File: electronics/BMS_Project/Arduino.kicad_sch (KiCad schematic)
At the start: 8 parts, among them SW1 SW_Push, SW3 SW_Push, SW4 SW_Push, SW5 SW_Push

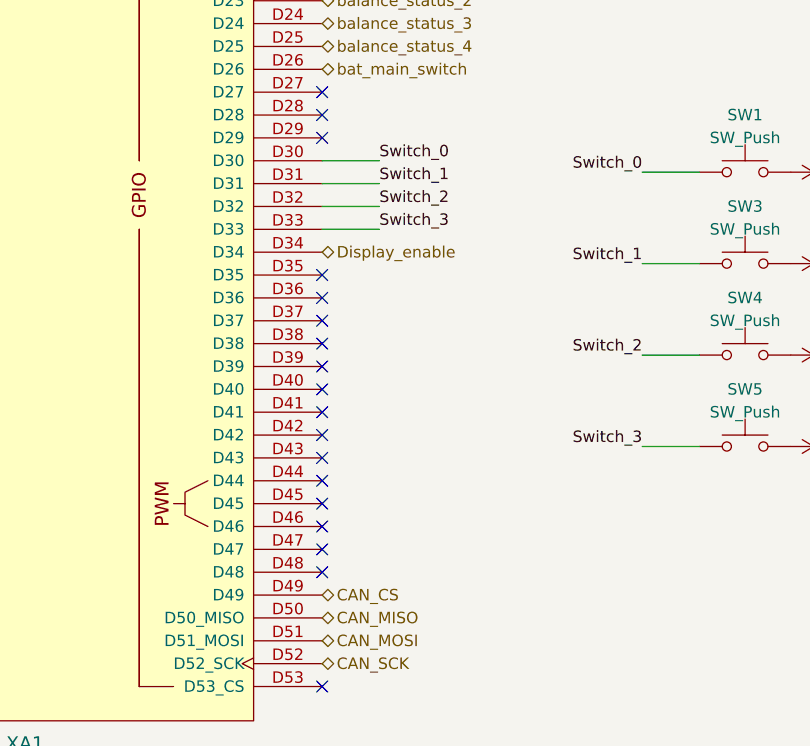
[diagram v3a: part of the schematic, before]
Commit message: Started PCB layout and adjusted schematic to suit the layout needs better
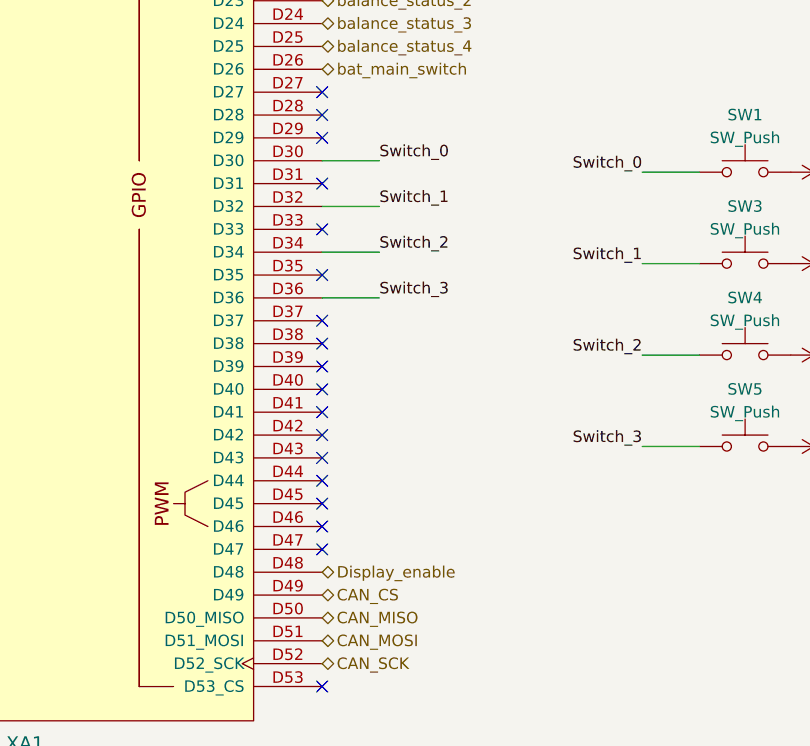
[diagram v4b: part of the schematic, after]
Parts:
- R13: footprint Resistor_THT:R_Axial_DIN0207_L6.3mm_D2.5mm_P10.16mm_Horizontal -> Resistor_SMD:R_0805_2012Metric
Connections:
- net Display_enable: now also XA1.D48; no longer XA1.D34
- net Switch_1: now also XA1.D32; no longer XA1.D31
- net Switch_2: now also XA1.D34; no longer XA1.D32
- net Switch_3: now also XA1.D36; no longer XA1.D33
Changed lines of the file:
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@@
   (no_connect (at 82.55 99.06))
   (no_connect (at 148.59 109.22))
-  (no_connect (at 148.59 137.16))
+  (no_connect (at 148.59 93.98))
   (no_connect (at 119.38 29.21))
   (no_connect (at 111.76 29.21))
@@
   (no_connect (at 148.59 53.34))
   (no_connect (at 109.22 29.21))
-  (no_connect (at 148.59 106.68))
   (no_connect (at 82.55 101.6))
   (no_connect (at 82.55 111.76))
@@
   (no_connect (at 148.59 149.86))
   (no_connect (at 148.59 114.3))
+  (no_connect (at 148.59 99.06))
   (wire (pts (xy 82.55 139.7) (xy 82.55 142.24))
     (stroke (width 0) (type default))
   )
+  (wire (pts (xy 148.59 101.6) (xy 154.94 101.6))
+    (stroke (width 0) (type default))
+  )
+  (wire (pts (xy 190.5 92.71) (xy 184.15 92.71))
+    (stroke (width 0) (type default))
+  )
+  (wire (pts (xy 148.59 91.44) (xy 154.94 91.44))
+    (stroke (width 0) (type default))
+  )
+  (wire (pts (xy 82.55 147.32) (xy 82.55 149.86))
+    (stroke (width 0) (type default))
+  )
+  (wire (pts (xy 66.04 114.3) (xy 69.85 114.3))
+    (stroke (width 0) (type default))
+  )
+  (wire (pts (xy 190.5 113.03) (xy 184.15 113.03))
+    (stroke (width 0) (type default))
+  )
+  (wire (pts (xy 72.39 137.16) (xy 82.55 137.16))
+    (stroke (width 0) (type default))
+  )
   (wire (pts (xy 148.59 96.52) (xy 154.94 96.52))
     (stroke (width 0) (type default))
   )
-  (wire (pts (xy 190.5 92.71) (xy 184.15 92.71))
-    (stroke (width 0) (type default))
-  )
-  (wire (pts (xy 148.59 91.44) (xy 154.94 91.44))
-    (stroke (width 0) (type default))
-  )
-  (wire (pts (xy 82.55 147.32) (xy 82.55 149.86))
-    (stroke (width 0) (type default))
-  )
-  (wire (pts (xy 66.04 114.3) (xy 69.85 114.3))
-    (stroke (width 0) (type default))
-  )
-  (wire (pts (xy 190.5 113.03) (xy 184.15 113.03))
-    (stroke (width 0) (type default))
-  )
-  (wire (pts (xy 72.39 137.16) (xy 82.55 137.16))
-    (stroke (width 0) (type default))
-  )
-  (wire (pts (xy 148.59 93.98) (xy 154.94 93.98))
-    (stroke (width 0) (type default))
-  )
   (wire (pts (xy 58.42 93.98) (xy 62.23 93.98))
     (stroke (width 0) (type default))
@@
     (stroke (width 0) (type default))
   )
-  (wire (pts (xy 148.59 99.06) (xy 154.94 99.06))
+  (wire (pts (xy 148.59 106.68) (xy 154.94 106.68))
     (stroke (width 0) (type default))
   )
@@
     (effects (font (size 1.27 1.27)) (justify right bottom))
   )
-  (label "Switch_1" (at 154.94 93.98 0) (fields_autoplaced)
+  (label "Switch_1" (at 154.94 96.52 0) (fields_autoplaced)
     (effects (font (size 1.27 1.27)) (justify left bottom))
   )
@@
     (effects (font (size 1.27 1.27)) (justify left bottom))
   )
-  (label "Switch_2" (at 154.94 96.52 0) (fields_autoplaced)
+  (label "Switch_2" (at 154.94 101.6 0) (fields_autoplaced)
     (effects (font (size 1.27 1.27)) (justify left bottom))
   )
@@
     (effects (font (size 1.27 1.27)) (justify right bottom))
   )
-  (label "Switch_3" (at 154.94 99.06 0) (fields_autoplaced)
+  (label "Switch_3" (at 154.94 106.68 0) (fields_autoplaced)
     (effects (font (size 1.27 1.27)) (justify left bottom))
   )
@@
     (effects (font (size 1.27 1.27)) (justify left))
   )
-  (hierarchical_label "Display_enable" (shape bidirectional) (at 148.59 101.6 0) (fields_autoplaced)
+  (hierarchical_label "Display_enable" (shape bidirectional) (at 148.59 137.16 0) (fields_autoplaced)
     (effects (font (size 1.27 1.27)) (justify left))
   )
@@
       (effects (font (size 1.27 1.27)))
     )
-    (property "Footprint" "Resistor_THT:R_Axial_DIN0207_L6.3mm_D2.5mm_P10.16mm_Horizontal" (at 54.61 92.202 90)
-      (effects (font (size 1.27 1.27)) hide)
-    )
+    (property "Footprint" "Resistor_SMD:R_0805_2012Metric" (at 54.61 92.202 90)
+      (effects (font (size 1.27 1.27)) hide)
+    )

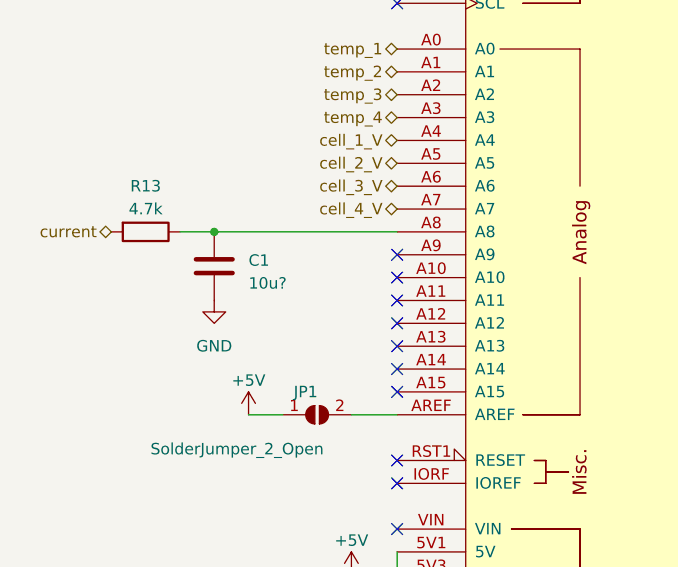
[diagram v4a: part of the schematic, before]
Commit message: changed the value of one capacitor
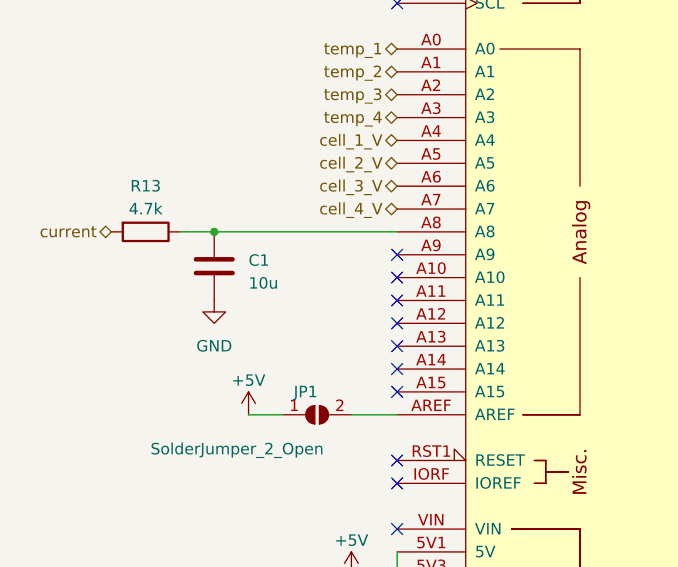
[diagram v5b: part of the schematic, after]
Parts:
- C1: value 10u? -> 10u
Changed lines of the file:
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@@
       (effects (font (size 1.27 1.27)) (justify left))
     )
-    (property "Value" "10u?" (at 66.04 99.695 0)
+    (property "Value" "10u" (at 66.04 99.695 0)
       (effects (font (size 1.27 1.27)) (justify left))
     )
